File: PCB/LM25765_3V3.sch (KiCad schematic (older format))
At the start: 8 parts

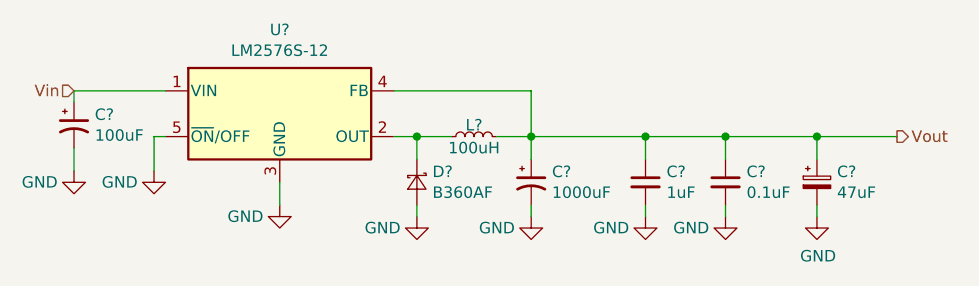
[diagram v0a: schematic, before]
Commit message: Added 3V3 regulator
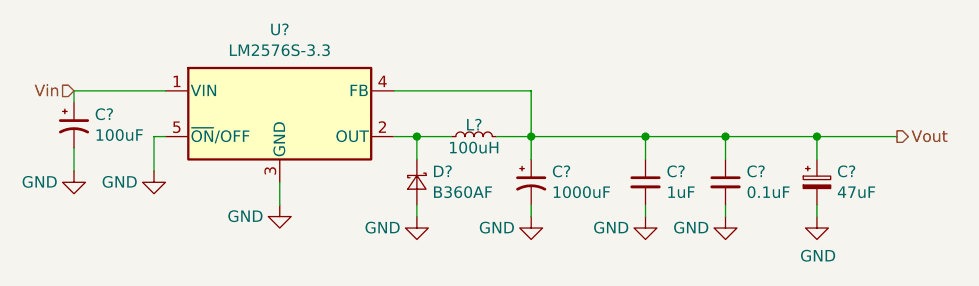
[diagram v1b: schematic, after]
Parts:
- U?: value LM2576S-12 -> LM2576S-3.3

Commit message: Cleanup
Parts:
- U?: value LM2576S-3.3 -> LM2576S-12
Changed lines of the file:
@@
 AR Path="/5E880E11/5E9C913B/5B713F8D" Ref="U?"  Part="1"
 F 0 "U?" H 5200 4117 50  0000 C CNN
-F 1 "LM2576S-3.3" H 5200 4026 50  0000 C CNN
+F 1 "LM2576S-12" H 5200 4026 50  0000 C CNN
 F 2 "Package_TO_SOT_SMD:TO-263-5_TabPin3" H 5200 3500 50  0001 L CIN
 F 3 "http://www.ti.com/lit/ds/symlink/lm2576.pdf" H 5200 3750 50  0001 C CNN

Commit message: Annotated Schematic
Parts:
- removed C59: 47uF, Capacitor_SMD:CP_Elec_4x5.4, symbol Device:CP_Small
- removed C?: 100uF, Capacitor_SMD:CP_Elec_5x5.4, symbol Device:CP1_Small
- added C23: 100uF, Capacitor_SMD:CP_Elec_5x5.4, symbol Device:CP1_Small
- added C27: 47uF, Capacitor_SMD:CP_Elec_4x5.4, symbol Device:CP_Small
- gave numbers to parts that had none: 4
- renumbered C57 to C25, C58 to C26
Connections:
- net GND: now also C23.2, C27.2
- net Vin: now also C23.1
- net Vout: now also C27.1
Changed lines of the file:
@@
 AR Path="/5E880E11/5E904307/5B713F64" Ref="#PWR?"  Part="1"
 AR Path="/5E880E11/5E9C764B/5B713F64" Ref="#PWR?"  Part="1"
-AR Path="/5E880E11/5E9C913B/5B713F64" Ref="#PWR?"  Part="1"
-F 0 "#PWR?" H 5200 3900 50  0001 C CNN
+AR Path="/5E880E11/5E9C913B/5B713F64" Ref="#PWR074"  Part="1"
+F 0 "#PWR074" H 5200 3900 50  0001 C CNN
 F 1 "GND" H 5050 4100 50  0000 C CNN
 F 2 "" H 5200 4150 50  0001 C CNN
@@
 AR Path="/5E880E11/5E904307/5B713F8D" Ref="U?"  Part="1"
 AR Path="/5E880E11/5E9C764B/5B713F8D" Ref="U?"  Part="1"
-AR Path="/5E880E11/5E9C913B/5B713F8D" Ref="U?"  Part="1"
-F 0 "U?" H 5200 4117 50  0000 C CNN
+AR Path="/5E880E11/5E9C913B/5B713F8D" Ref="U5"  Part="1"
+F 0 "U5" H 5200 4117 50  0000 C CNN
 F 1 "LM2576S-12" H 5200 4026 50  0000 C CNN
 F 2 "Package_TO_SOT_SMD:TO-263-5_TabPin3" H 5200 3500 50  0001 L CIN
@@
 AR Path="/5E880E11/5E904307/5B713FA0" Ref="C?"  Part="1"
 AR Path="/5E880E11/5E9C764B/5B713FA0" Ref="C?"  Part="1"
-AR Path="/5E880E11/5E9C913B/5B713FA0" Ref="C?"  Part="1"
-F 0 "C?" H 6391 4096 50  0000 L CNN
+AR Path="/5E880E11/5E9C913B/5B713FA0" Ref="C24"  Part="1"
+F 0 "C24" H 6391 4096 50  0000 L CNN
 F 1 "1000uF" H 6391 4005 50  0000 L CNN
 F 2 "Capacitor_SMD:CP_Elec_8x10" H 6300 4050 50  0001 C CNN
-F 3 "~" H 6300 4050 50  0001 C CNN
+F 3 "" H 6300 4050 50  0001 C CNN
 F 4 "UWT0J102MNL1GS" H 6300 4050 50  0001 C CNN "MPN"
 F 5 "Power Supply" H 6300 4050 50  0001 C CNN "Functional Block"
@@
 AR Path="/5E880E11/5E904307/5B713FAA" Ref="#PWR?"  Part="1"
 AR Path="/5E880E11/5E9C764B/5B713FAA" Ref="#PWR?"  Part="1"
-AR Path="/5E880E11/5E9C913B/5B713FAA" Ref="#PWR?"  Part="1"
-F 0 "#PWR?" H 6300 3950 50  0001 C CNN
+AR Path="/5E880E11/5E9C913B/5B713FAA" Ref="#PWR076"  Part="1"
+F 0 "#PWR076" H 6300 3950 50  0001 C CNN
 F 1 "GND" H 6150 4150 50  0000 C CNN
 F 2 "" H 6300 4200 50  0001 C CNN
@@
 AR Path="/5E880E11/5E904307/5B713FB1" Ref="L?"  Part="1"
 AR Path="/5E880E11/5E9C764B/5B713FB1" Ref="L?"  Part="1"
-AR Path="/5E880E11/5E9C913B/5B713FB1" Ref="L?"  Part="1"
-F 0 "L?" V 6100 3850 50  0000 C CNN
+AR Path="/5E880E11/5E9C913B/5B713FB1" Ref="L1"  Part="1"
+F 0 "L1" V 6100 3850 50  0000 C CNN
 F 1 "100uH" V 6000 3850 50  0000 C CNN
 F 2 "Inductor_SMD:L_Wuerth_WE-PD-Typ-LS_Handsoldering" H 6050 3850 50  0001 C CNN
@@
 AR Path="/5E880E11/5E904307/5B713FBB" Ref="#PWR?"  Part="1"
 AR Path="/5E880E11/5E9C764B/5B713FBB" Ref="#PWR?"  Part="1"
-AR Path="/5E880E11/5E9C913B/5B713FBB" Ref="#PWR?"  Part="1"
-F 0 "#PWR?" H 5800 3950 50  0001 C CNN
+AR Path="/5E880E11/5E9C913B/5B713FBB" Ref="#PWR075"  Part="1"
+F 0 "#PWR075" H 5800 3950 50  0001 C CNN
 F 1 "GND" H 5650 4150 50  0000 C CNN
 F 2 "" H 5800 4200 50  0001 C CNN
@@
 AR Path="/5E880E11/5E904307/5B713FDF" Ref="D?"  Part="1"
 AR Path="/5E880E11/5E9C764B/5B713FDF" Ref="D?"  Part="1"
-AR Path="/5E880E11/5E9C913B/5B713FDF" Ref="D?"  Part="1"
-F 0 "D?" V 5754 4118 50  0000 L CNN
+AR Path="/5E880E11/5E9C913B/5B713FDF" Ref="D6"  Part="1"
+F 0 "D6" V 5754 4118 50  0000 L CNN
 F 1 "B360AF" V 5845 4118 50  0000 L CNN
 F 2 "Diode_SMD:D_SMA" V 5800 4050 50  0001 C CNN
-F 3 "~" V 5800 4050 50  0001 C CNN
+F 3 "" V 5800 4050 50  0001 C CNN
 F 4 "B360AF-13" V 5800 4050 50  0001 C CNN "MPN"
 F 5 "Diodes Incorporated" V 5800 4050 50  0001 C CNN "Manufacturer"
@@
 P 6800 4050
 AR Path="/5B9CEDF5" Ref="C?"  Part="1"
-AR Path="/5B713D50/5B9CEDF5" Ref="C57"  Part="1"
+AR Path="/5B713D50/5B9CEDF5" Ref="C?"  Part="1"
 AR Path="/5E880E11/5E904307/5B9CEDF5" Ref="C?"  Part="1"
 AR Path="/5E880E11/5E9C764B/5B9CEDF5" Ref="C?"  Part="1"
-AR Path="/5E880E11/5E9C913B/5B9CEDF5" Ref="C?"  Part="1"
-F 0 "C?" H 6892 4096 50  0000 L CNN
+AR Path="/5E880E11/5E9C913B/5B9CEDF5" Ref="C25"  Part="1"
+F 0 "C25" H 6892 4096 50  0000 L CNN
 F 1 "1uF" H 6892 4005 50  0000 L CNN
 F 2 "Capacitors:0603" H 6800 4050 50  0001 C CNN
-F 3 "~" H 6800 4050 50  0001 C CNN
+F 3 "" H 6800 4050 50  0001 C CNN
 F 4 "Power Supply" H 6800 4050 50  0001 C CNN "Functional Block"
 F 5 "X7R" H -700 -100 50  0001 C CNN "Dielectric"
@@
 P 7150 4050
 AR Path="/5B9CEDFC" Ref="C?"  Part="1"
-AR Path="/5B713D50/5B9CEDFC" Ref="C58"  Part="1"
+AR Path="/5B713D50/5B9CEDFC" Ref="C?"  Part="1"
 AR Path="/5E880E11/5E904307/5B9CEDFC" Ref="C?"  Part="1"
 AR Path="/5E880E11/5E9C764B/5B9CEDFC" Ref="C?"  Part="1"
-AR Path="/5E880E11/5E9C913B/5B9CEDFC" Ref="C?"  Part="1"
-F 0 "C?" H 7242 4096 50  0000 L CNN
+AR Path="/5E880E11/5E9C913B/5B9CEDFC" Ref="C26"  Part="1"
+F 0 "C26" H 7242 4096 50  0000 L CNN
 F 1 "0.1uF" H 7242 4005 50  0000 L CNN
 F 2 "Capacitors:0603" H 7150 4050 50  0001 C CNN
-F 3 "~" H 7150 4050 50  0001 C CNN
+F 3 "" H 7150 4050 50  0001 C CNN
 F 4 "Power Supply" H 7150 4050 50  0001 C CNN "Functional Block"
 F 5 "X7R" H -700 -100 50  0001 C CNN "Dielectric"
@@
 $Comp
 L power:GND #PWR?
-U 1 1 5B9CEE03
+U 1 1 5E8CA26E
 P 7550 4200
-AR Path="/5B9CEE03" Ref="#PWR?"  Part="1"
-AR Path="/5B713D50/5B9CEE03" Ref="#PWR0137"  Part="1"
-AR Path="/5E880E11/5E904307/5B9CEE03" Ref="#PWR?"  Part="1"
-AR Path="/5E880E11/5E9C764B/5B9CEE03" Ref="#PWR?"  Part="1"
-AR Path="/5E880E11/5E9C913B/5B9CEE03" Ref="#PWR?"  Part="1"
-F 0 "#PWR?" H 7550 3950 50  0001 C CNN
+AR Path="/5E8CA26E" Ref="#PWR?"  Part="1"
+AR Path="/5B713D50/5E8CA26E" Ref="#PWR?"  Part="1"
+AR Path="/5E880E11/5E904307/5E8CA26E" Ref="#PWR?"  Part="1"
+AR Path="/5E880E11/5E9C764B/5E8CA26E" Ref="#PWR?"  Part="1"
+AR Path="/5E880E11/5E9C913B/5E8CA26E" Ref="#PWR079"  Part="1"
+F 0 "#PWR079" H 7550 3950 50  0001 C CNN
 F 1 "GND" H 7555 4027 50  0000 C CNN
 F 2 "" H 7550 4200 50  0001 C CNN
@@
 $Comp
 L Device:CP_Small C?
-U 1 1 5B9CEE1A
+U 1 1 5E8CA26F
 P 7550 4050
-AR Path="/5B9CEE1A" Ref="C?"  Part="1"
-AR Path="/5B713D50/5B9CEE1A" Ref="C59"  Part="1"
-AR Path="/5E880E11/5E904307/5B9CEE1A" Ref="C?"  Part="1"
-AR Path="/5E880E11/5E9C764B/5B9CEE1A" Ref="C?"  Part="1"
-AR Path="/5E880E11/5E9C913B/5B9CEE1A" Ref="C?"  Part="1"
-F 0 "C?" H 7638 4096 50  0000 L CNN
+AR Path="/5E8CA26F" Ref="C?"  Part="1"
+AR Path="/5B713D50/5E8CA26F" Ref="C?"  Part="1"
+AR Path="/5E880E11/5E904307/5E8CA26F" Ref="C?"  Part="1"
+AR Path="/5E880E11/5E9C764B/5E8CA26F" Ref="C?"  Part="1"
+AR Path="/5E880E11/5E9C913B/5E8CA26F" Ref="C27"  Part="1"
+F 0 "C27" H 7638 4096 50  0000 L CNN
 F 1 "47uF" H 7638 4005 50  0000 L CNN
 F 2 "Capacitor_SMD:CP_Elec_4x5.4" H 7550 4050 50  0001 C CNN
-F 3 "~" H 7550 4050 50  0001 C CNN
+F 3 "" H 7550 4050 50  0001 C CNN
 F 4 "EEE-0JA470WR" H -700 -100 50  0001 C CNN "MPN"
 F 5 "Panasonic" H -700 -100 50  0001 C CNN "Manufacturer"
@@
 $Comp
 L power:GND #PWR?
-U 1 1 5B9D0690
+U 1 1 5E8CA270
 P 6800 4200
-AR Path="/5E880E11/5E904307/5B9D0690" Ref="#PWR?"  Part="1"
-AR Path="/5E880E11/5E9C764B/5B9D0690" Ref="#PWR?"  Part="1"
-AR Path="/5E880E11/5E9C913B/5B9D0690" Ref="#PWR?"  Part="1"
-F 0 "#PWR?" H 6800 3950 50  0001 C CNN
+AR Path="/5E880E11/5E904307/5E8CA270" Ref="#PWR?"  Part="1"
+AR Path="/5E880E11/5E9C764B/5E8CA270" Ref="#PWR?"  Part="1"
+AR Path="/5E880E11/5E9C913B/5E8CA270" Ref="#PWR077"  Part="1"
+F 0 "#PWR077" H 6800 3950 50  0001 C CNN
 F 1 "GND" H 6650 4150 50  0000 C CNN
 F 2 "" H 6800 4200 50  0001 C CNN
@@
 $Comp
 L power:GND #PWR?
-U 1 1 5B9D06AF
+U 1 1 5E8CA271
 P 7150 4200
-AR Path="/5E880E11/5E904307/5B9D06AF" Ref="#PWR?"  Part="1"
-AR Path="/5E880E11/5E9C764B/5B9D06AF" Ref="#PWR?"  Part="1"
-AR Path="/5E880E11/5E9C913B/5B9D06AF" Ref="#PWR?"  Part="1"
-F 0 "#PWR?" H 7150 3950 50  0001 C CNN
+AR Path="/5E880E11/5E904307/5E8CA271" Ref="#PWR?"  Part="1"
+AR Path="/5E880E11/5E9C764B/5E8CA271" Ref="#PWR?"  Part="1"
+AR Path="/5E880E11/5E9C913B/5E8CA271" Ref="#PWR078"  Part="1"
+F 0 "#PWR078" H 7150 3950 50  0001 C CNN
 F 1 "GND" H 7000 4150 50  0000 C CNN
 F 2 "" H 7150 4200 50  0001 C CNN
@@
 $Comp
 L power:GND #PWR?
-U 1 1 5B713FC7
+U 1 1 5E8CA268
 P 4650 4000
-AR Path="/5E880E11/5E904307/5B713FC7" Ref="#PWR?"  Part="1"
-AR Path="/5E880E11/5E9C764B/5B713FC7" Ref="#PWR?"  Part="1"
-AR Path="/5E880E11/5E9C913B/5B713FC7" Ref="#PWR?"  Part="1"
-F 0 "#PWR?" H 4650 3750 50  0001 C CNN
+AR Path="/5E880E11/5E904307/5E8CA268" Ref="#PWR?"  Part="1"
+AR Path="/5E880E11/5E9C764B/5E8CA268" Ref="#PWR?"  Part="1"
+AR Path="/5E880E11/5E9C913B/5E8CA268" Ref="#PWR073"  Part="1"
+F 0 "#PWR073" H 4650 3750 50  0001 C CNN
 F 1 "GND" H 4500 3950 50  0000 C CNN
 F 2 "" H 4650 4000 50  0001 C CNN
@@
 $Comp
 L power:GND #PWR?
-U 1 1 5B713FD6
+U 1 1 5E8CA26A
 P 4300 4000
-AR Path="/5E880E11/5E904307/5B713FD6" Ref="#PWR?"  Part="1"
-AR Path="/5E880E11/5E9C764B/5B713FD6" Ref="#PWR?"  Part="1"
-AR Path="/5E880E11/5E9C913B/5B713FD6" Ref="#PWR?"  Part="1"
-F 0 "#PWR?" H 4300 3750 50  0001 C CNN
+AR Path="/5E880E11/5E904307/5E8CA26A" Ref="#PWR?"  Part="1"
+AR Path="/5E880E11/5E9C764B/5E8CA26A" Ref="#PWR?"  Part="1"
+AR Path="/5E880E11/5E9C913B/5E8CA26A" Ref="#PWR072"  Part="1"
+F 0 "#PWR072" H 4300 3750 50  0001 C CNN
 F 1 "GND" H 4150 3950 50  0000 C CNN
 F 2 "" H 4300 4000 50  0001 C CNN
@@
 $Comp
 L Device:CP1_Small C?
-U 1 1 5B713FCF
+U 1 1 5E8CA269
 P 4300 3800
-AR Path="/5E880E11/5E904307/5B713FCF" Ref="C?"  Part="1"
-AR Path="/5E880E11/5E9C764B/5B713FCF" Ref="C?"  Part="1"
-AR Path="/5E880E11/5E9C913B/5B713FCF" Ref="C?"  Part="1"
-F 0 "C?" H 4391 3846 50  0000 L CNN
+AR Path="/5E880E11/5E904307/5E8CA269" Ref="C?"  Part="1"
+AR Path="/5E880E11/5E9C764B/5E8CA269" Ref="C?"  Part="1"
+AR Path="/5E880E11/5E9C913B/5E8CA269" Ref="C23"  Part="1"
+F 0 "C23" H 4391 3846 50  0000 L CNN
 F 1 "100uF" H 4391 3755 50  0000 L CNN
 F 2 "Capacitor_SMD:CP_Elec_5x5.4" H 4300 3800 50  0001 C CNN
-F 3 "~" H 4300 3800 50  0001 C CNN
+F 3 "" H 4300 3800 50  0001 C CNN
 F 4 "EEE-1AA101SP" H 0   0   50  0001 C CNN "MPN"
 F 5 "Panasonic" H 0   0   50  0001 C CNN "Manufacturer"

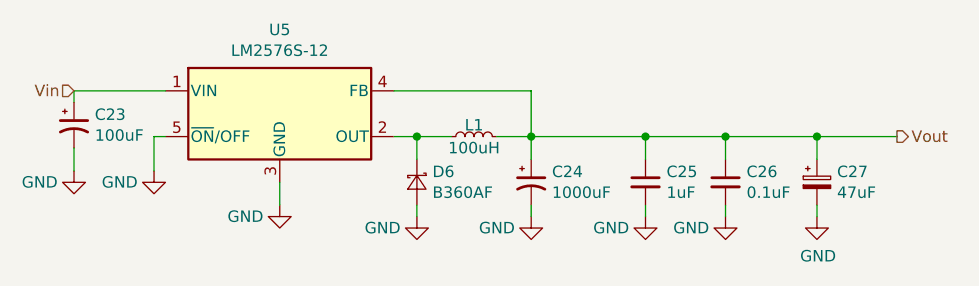
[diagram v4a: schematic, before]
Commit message: Added Dielectric and voltage rating to all capacitors
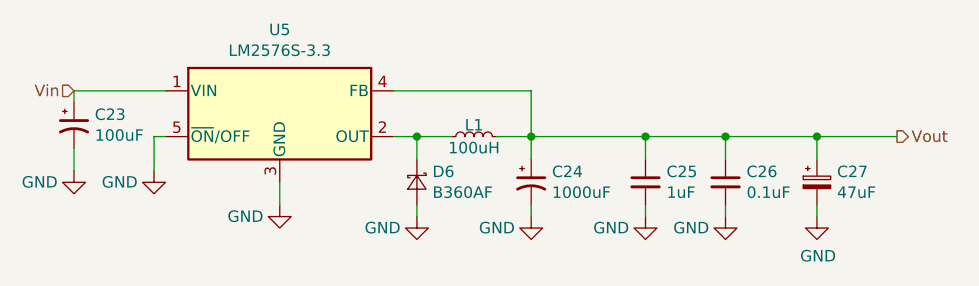
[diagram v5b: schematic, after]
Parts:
- C25, C26: Voltage Rating (none) -> 6.3V
- U5: value LM2576S-12 -> LM2576S-3.3
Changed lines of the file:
@@
 AR Path="/5E880E11/5E9C913B/5B713F8D" Ref="U5"  Part="1"
 F 0 "U5" H 5200 4117 50  0000 C CNN
-F 1 "LM2576S-12" H 5200 4026 50  0000 C CNN
+F 1 "LM2576S-3.3" H 5200 4026 50  0000 C CNN
 F 2 "Package_TO_SOT_SMD:TO-263-5_TabPin3" H 5200 3500 50  0001 L CIN
 F 3 "http://www.ti.com/lit/ds/symlink/lm2576.pdf" H 5200 3750 50  0001 C CNN
@@
 F 4 "Power Supply" H 6800 4050 50  0001 C CNN "Functional Block"
 F 5 "X7R" H -700 -100 50  0001 C CNN "Dielectric"
+F 6 "6.3V" H 6800 4050 50  0001 C CNN "Voltage Rating"
 	1    6800 4050
 	1    0    0    -1
@@
 F 4 "Power Supply" H 7150 4050 50  0001 C CNN "Functional Block"
 F 5 "X7R" H -700 -100 50  0001 C CNN "Dielectric"
+F 6 "6.3V" H 7150 4050 50  0001 C CNN "Voltage Rating"
 	1    7150 4050
 	1    0    0    -1
